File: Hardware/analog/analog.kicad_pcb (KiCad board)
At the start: 4 copper layers, 128 x 182 mm, 101 parts, among them J201 Würth 74651194R, J202 Würth 74651194R, J301 Conn_02x10_Odd_Even, J501 Conn_01x01, J502 Conn_01x01, M501 Fan_4pin, Q201 IXTH80N075L2, Q501 MMBT3904, U201 ADA4522-2, U202 LM431SC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

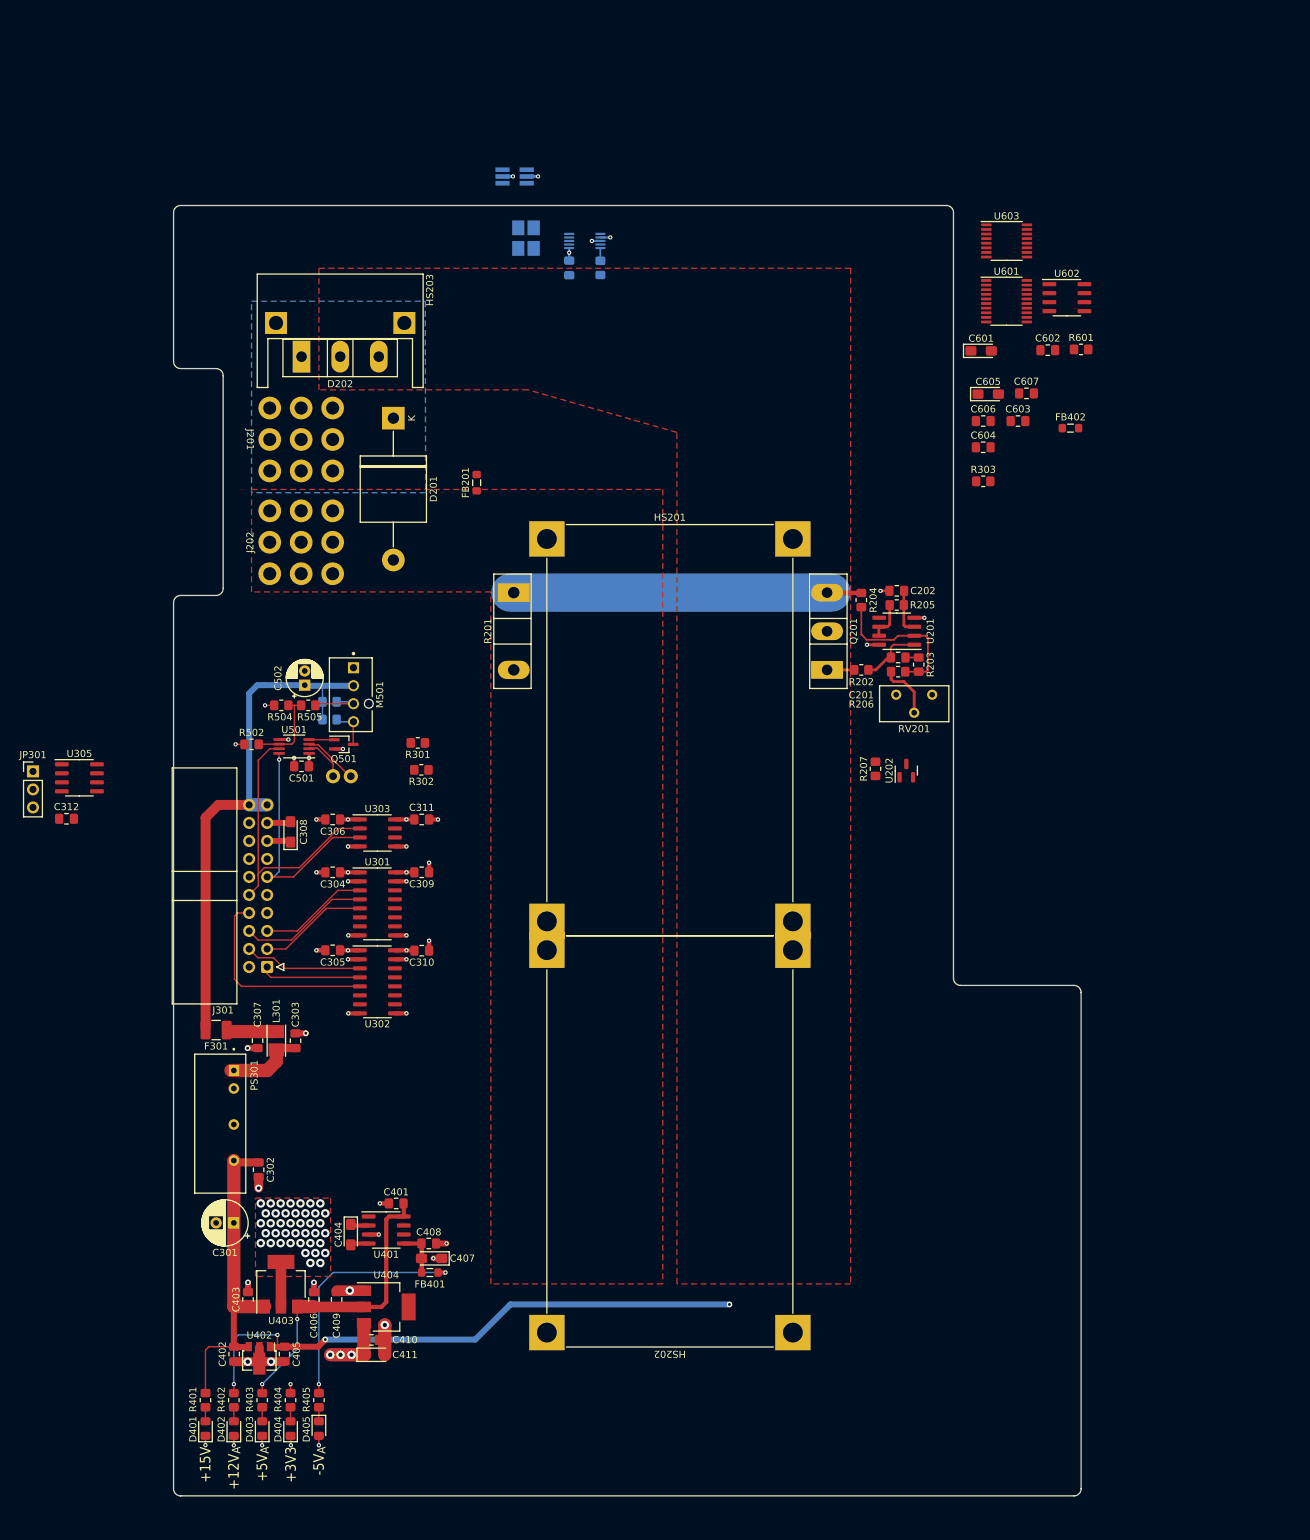
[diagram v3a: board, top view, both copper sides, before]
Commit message: Add ADC aliasing filters
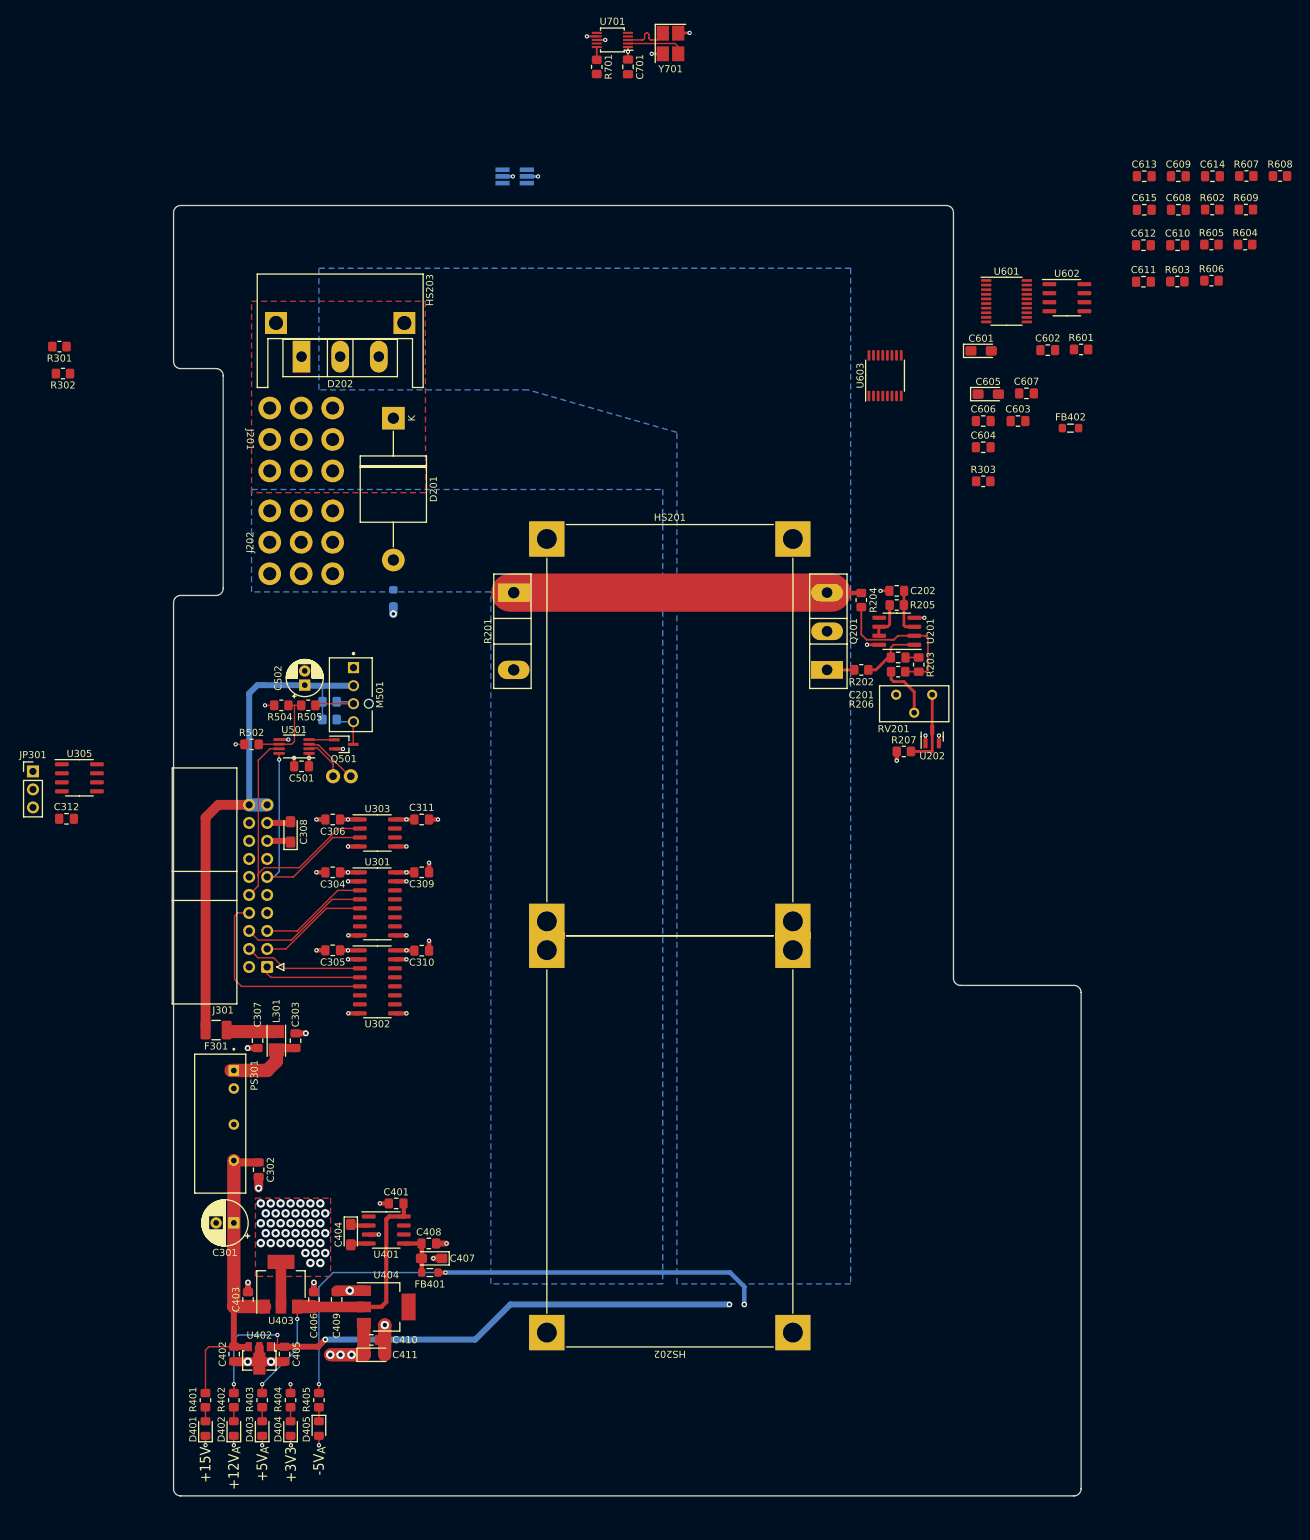
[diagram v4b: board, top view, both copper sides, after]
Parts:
- removed G***: LOGO, LOGO
- added C608: 100nF, Capacitor_SMD:C_0805_2012Metric_Pad1.18x1.45mm_HandSolder, F.Cu at (161.7, 20.6)
- added C609: 100nF, Capacitor_SMD:C_0805_2012Metric_Pad1.18x1.45mm_HandSolder, F.Cu at (161.7, 15.9)
- added C610: 100nF, Capacitor_SMD:C_0805_2012Metric_Pad1.18x1.45mm_HandSolder, F.Cu at (161.6, 25.6)
- added C611: 100nF, Capacitor_SMD:C_0805_2012Metric_Pad1.18x1.45mm_HandSolder, F.Cu at (156.8, 30.8)
- added C612: 100nF, Capacitor_SMD:C_0805_2012Metric_Pad1.18x1.45mm_HandSolder, F.Cu at (156.8, 25.6)
- added C613: 100nF, Capacitor_SMD:C_0805_2012Metric_Pad1.18x1.45mm_HandSolder, F.Cu at (156.9, 15.9)
- added C614: 100nF, Capacitor_SMD:C_0805_2012Metric_Pad1.18x1.45mm_HandSolder, F.Cu at (166.5, 15.9)
- added C615: 100nF, Capacitor_SMD:C_0805_2012Metric_Pad1.18x1.45mm_HandSolder, F.Cu at (156.9, 20.6)
- added R602: 1k, Resistor_SMD:R_0805_2012Metric_Pad1.20x1.40mm_HandSolder, F.Cu at (166.5, 20.6)
- added R603: 1k, Resistor_SMD:R_0805_2012Metric_Pad1.20x1.40mm_HandSolder, F.Cu at (161.6, 30.7)
- added R604: 1k, Resistor_SMD:R_0805_2012Metric_Pad1.20x1.40mm_HandSolder, F.Cu at (171.1, 25.5)
- added R605: 1k, Resistor_SMD:R_0805_2012Metric_Pad1.20x1.40mm_HandSolder, F.Cu at (166.4, 25.5)
- added R606: 1k, Resistor_SMD:R_0805_2012Metric_Pad1.20x1.40mm_HandSolder, F.Cu at (166.4, 30.6)
- added R607: 1k, Resistor_SMD:R_0805_2012Metric_Pad1.20x1.40mm_HandSolder, F.Cu at (171.3, 15.8)
- added R608: 1k, Resistor_SMD:R_0805_2012Metric_Pad1.20x1.40mm_HandSolder, F.Cu at (176.1, 15.8)
- added R609: 1k, Resistor_SMD:R_0805_2012Metric_Pad1.20x1.40mm_HandSolder, F.Cu at (171.2, 20.6)
- C701, R701, U701, Y701: moved to F.Cu
- FB201: moved to B.Cu
- moved R301 75.4 mm to (3.90, 39.9)
- moved R302 75.4 mm to (4.40, 43.7)
- moved Y701 34.2 mm to (90.1, -2.85), turned to -90 degrees
- moved C701 29.5 mm to (84.1, 0.45)
- moved U701 28.6 mm to (81.9, -3.35), turned to 180 degrees
- moved R701 28.4 mm to (79.7, 0.45)
- moved U603 25.6 mm to (120.3, 44.0), turned to 90 degrees
- moved FB201 20.1 mm to (51.0, 75.3), turned to -90 degrees
- moved U202 6.03 mm to (127.0, 94.9)
- moved R207 4.69 mm to (123.0, 97.0), turned to 180 degrees
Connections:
- net /Analog stuff/ISet_{1} renamed /ISet_{1
- net /Analog stuff/ISet_{2} renamed /ISet_{2
- net /Analog stuff/ISet_{3} renamed /ISet_{3
- R207 pad 2: -5V -> -5VA
- U201 pad 5: /MOSFET Load/DRIVE0 -> /ISet_{0
- U603 pad 1: /Analog stuff/ISet_{0} -> /ISet_{0
- Y701 pad 2: Net-(U701-Pad2) -> GND
- Y701 pad 3: (no net) -> Net-(U701-Pad2)
- Y701 pad 4: (no net) -> GND
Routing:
- net -5VA: track 34.7 -> 178.2 mm, vias 2 -> 4
- net Net-(R207-Pad1): track 0.00 -> 11.0 mm
- net Net-(U701-Pad2): track 0.00 -> 7.33 mm
- net GND: track 58.9 -> 65.5 mm, vias 68 -> 73
- net Net-(U701-Pad3): track 0.00 -> 5.74 mm
- added copper zone on B.Cu, net +VDC
- added copper zone on F.Cu, net /MOSFET Load/VBUS_IN
- added copper zone on B.Cu, net GNDPWR
- removed copper zone on F.Cu, net +VDC
- removed copper zone on B.Cu, net /MOSFET Load/VBUS_IN
- removed copper zone on F.Cu, net GNDPWR

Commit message: More tweaks to analog board
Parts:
- removed HS202: 2x C40-058-AE, programmable-load:C40-058-AE-DUAL
- added HS201: 2x C40-058-AE, programmable-load:C40-058-AE-DUAL, F.Cu at (70.0, 165.0)
- added U203: LMT86LMT, Package_TO_SOT_THT:TO-92_Inline_Wide, F.Cu at (112.1, 98.5)
